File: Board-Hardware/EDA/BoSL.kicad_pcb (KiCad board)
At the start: 2 copper layers, 88 x 69.8 mm, 57 parts, among them CON1 Micro_SD_Card, CON2 BARREL_JACK, IC1 ATMEGA328-P, IC2 SIM7000, J1 Screw_Terminal_1x06, J2 Screw_Terminal_1x04, J3 Screw_Terminal_1x02, J4 Screw_Terminal_1x08, J5 Screw_Terminal_1x04, J6 RJ45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

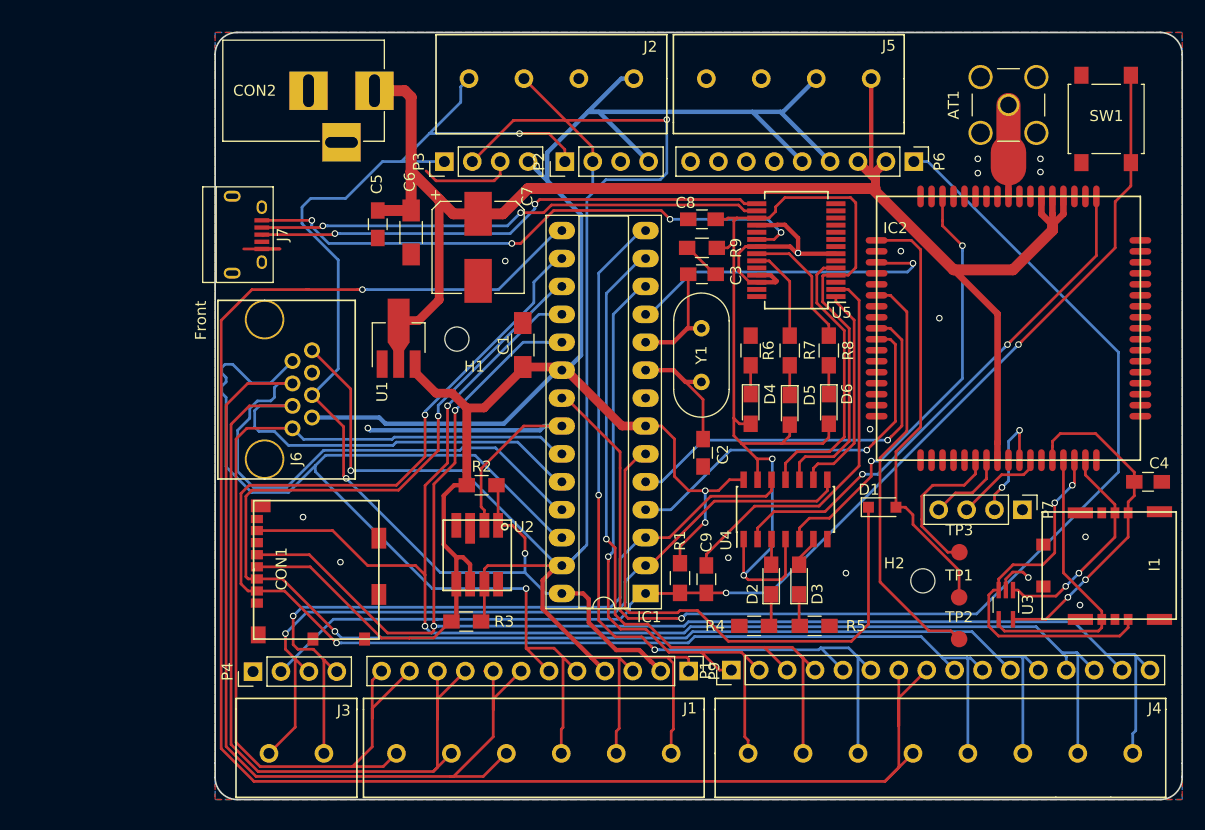
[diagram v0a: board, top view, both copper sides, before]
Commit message: renamed bosl GPS to bosl
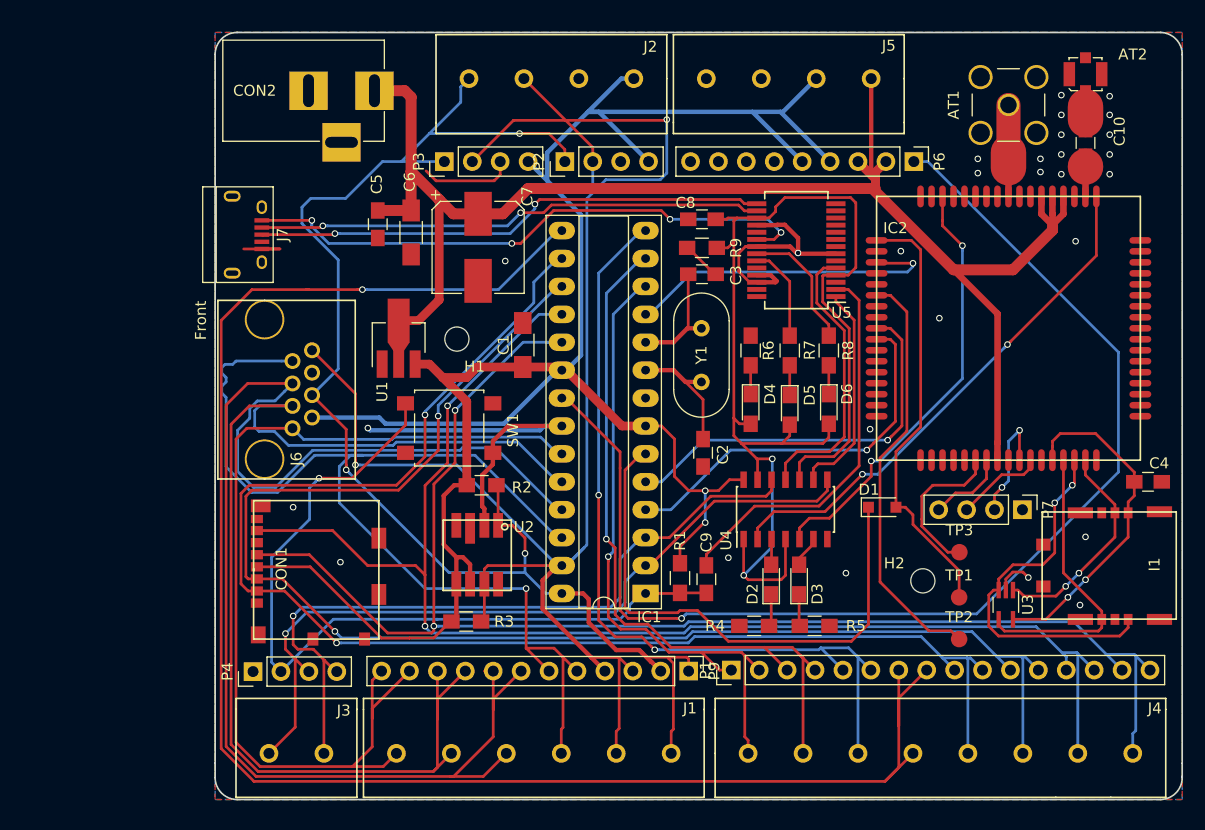
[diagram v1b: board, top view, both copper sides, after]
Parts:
- removed G***: LOGO, SIMFootprints:Logo
- added AT2: AT-GNSS, Connectors_Molex:Molex_Microcoaxial_RF, F.Cu at (183.7, 66.8)
- added C10: 33 pF, Capacitors_SMD:C_0805_HandSoldering, F.Cu at (183.7, 73.0)
- moved SW1 66.1 mm to (125.8, 99.0), turned to 180 degrees
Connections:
- IC2 pad 53: (no net) -> Net-(C10-Pad2)
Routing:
- net TLL_RST: track 108.9 -> 73.9 mm, vias 2 -> 1
- net Net-(C10-Pad2): track 0.00 -> 3.79 mm
- net V_3.3: track 197.0 -> 198.8 mm
- net Net-(AT2-Pad1): track 0.00 -> 1.17 mm
- net GND: track 75.3 -> 76.1 mm, vias 17 -> 28
- net SDA: track 155.6 -> 155.0 mm
- net A3: track 100.9 -> 101.4 mm
- net A2: track 128.5 -> 128.0 mm
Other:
- board text added: "Rev: 0.3 G Monash BoSL GSP Board"
- board text removed: "Rev: 0.3 Monash BoSL Board"

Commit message: begun layout of bosl board rev 0.4
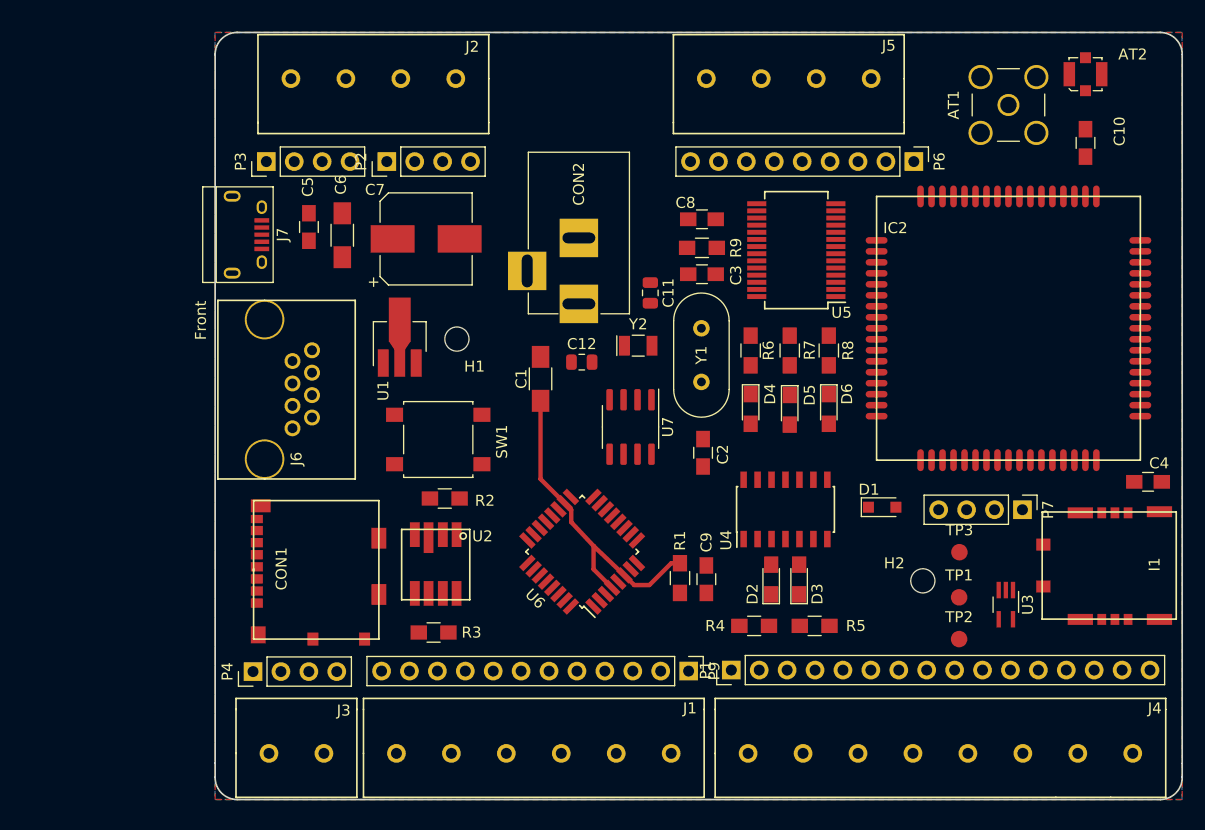
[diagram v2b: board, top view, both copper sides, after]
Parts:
- removed IC1: ATMEGA328-P, Housings_DIP:DIP-28_W7.62mm_Socket_LongPads
- added C11: 12 pF, Capacitor_SMD:C_0805_2012Metric, F.Cu at (144.1, 86.7)
- added C12: 12 pF, Capacitor_SMD:C_0805_2012Metric, F.Cu at (137.9, 93.0)
- added U6: ATmega328P-AU, Package_QFP:TQFP-32_7x7mm_P0.8mm, F.Cu at (137.9, 110.2)
- added U7: MCP7940N-xSN, Package_SO:SOIC-8_3.9x4.9mm_P1.27mm, F.Cu at (142.3, 98.9)
- added Y2: 32.768 kHz, Crystal:Crystal_SMD_EuroQuartz_EQ161-2Pin_3.2x1.5mm, F.Cu at (143.0, 91.5)
- moved CON2 26.9 mm to (137.6, 87.7), turned to 270 degrees
- moved P2 16.2 mm to (120.1, 74.8)
- moved P3 16.2 mm to (109.2, 74.8)
- moved J2 16.2 mm to (126.4, 67.2)
- moved C6 6.27 mm to (116.1, 81.5)
- moved C5 6.27 mm to (113.0, 80.7)
- moved C7 4.79 mm to (123.7, 81.8), turned to 0 degrees
- moved U2 3.87 mm to (124.5, 111.4)
- moved R2 3.57 mm to (125.4, 105.4)
- moved C1 3.48 mm to (134.1, 94.5)
- moved R3 3.13 mm to (124.4, 117.6)
- moved SW1 1.44 mm to (124.8, 100.0)
- moved U1 0.14 mm to (121.3, 91.1)
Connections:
- CON1 pad 1: (no net) -> Net-(CON1-Pad1)
- CON1 pad 8: (no net) -> Net-(CON1-Pad8)
- I1 pad 5: (no net) -> Net-(I1-Pad5)
- IC2 pad 11: (no net) -> Net-(IC2-Pad11)
- IC2 pad 12: (no net) -> Net-(IC2-Pad12)
- IC2 pad 13: (no net) -> Net-(IC2-Pad13)
- IC2 pad 14: (no net) -> Net-(IC2-Pad14)
- IC2 pad 15: (no net) -> Net-(IC2-Pad15)
- IC2 pad 16: (no net) -> Net-(IC2-Pad16)
- IC2 pad 19: (no net) -> Net-(IC2-Pad19)
- IC2 pad 20: (no net) -> Net-(IC2-Pad20)
- IC2 pad 21: (no net) -> Net-(IC2-Pad21)
- IC2 pad 22: (no net) -> Net-(IC2-Pad22)
- IC2 pad 26: (no net) -> Net-(IC2-Pad26)
- IC2 pad 34: (no net) -> Net-(IC2-Pad34)
- IC2 pad 35: (no net) -> Net-(IC2-Pad35)
- IC2 pad 36: (no net) -> Net-(IC2-Pad36)
- IC2 pad 37: (no net) -> Net-(IC2-Pad37)
- IC2 pad 38: (no net) -> Net-(IC2-Pad38)
- IC2 pad 4: (no net) -> Net-(IC2-Pad4)
- IC2 pad 40: (no net) -> Net-(IC2-Pad40)
- IC2 pad 41: (no net) -> Net-(IC2-Pad41)
- IC2 pad 42: (no net) -> Net-(IC2-Pad42)
- IC2 pad 43: (no net) -> Net-(IC2-Pad43)
- IC2 pad 44: (no net) -> Net-(IC2-Pad44)
- IC2 pad 47: (no net) -> Net-(IC2-Pad47)
- IC2 pad 48: (no net) -> Net-(IC2-Pad48)
- IC2 pad 49: (no net) -> Net-(IC2-Pad49)
- IC2 pad 5: (no net) -> Net-(IC2-Pad5)
- IC2 pad 50: (no net) -> Net-(IC2-Pad50)
- IC2 pad 51: (no net) -> Net-(IC2-Pad51)
- IC2 pad 67: (no net) -> Net-(IC2-Pad67)
- IC2 pad 68: (no net) -> Net-(IC2-Pad68)
- IC2 pad 7: (no net) -> Net-(IC2-Pad7)
- IC2 pad 8: (no net) -> Net-(IC2-Pad8)
- J4 pad 1: D6 -> D2
- J4 pad 2: D7 -> D3
- J4 pad 3: D8 -> D6
- J4 pad 4: D9 -> D7
- J7 pad 4: (no net) -> Net-(J7-Pad4)
- J7 pad 6: (no net) -> Net-(J7-Pad6)
- P1 pad 1: D6 -> D2
- P1 pad 2: D6 -> D2
- P1 pad 3: D7 -> D3
- P1 pad 4: D7 -> D3
- P1 pad 5: D8 -> D6
- P1 pad 6: D8 -> D6
- P1 pad 7: D9 -> D7
- P1 pad 8: D9 -> D7
- U2 pad 4: (no net) -> Net-(U2-Pad4)
- U2 pad 8: (no net) -> Net-(U2-Pad8)
- U5 pad 10: (no net) -> Net-(U5-Pad10)
- U5 pad 11: (no net) -> Net-(U5-Pad11)
- U5 pad 12: (no net) -> Net-(U5-Pad12)
- U5 pad 13: (no net) -> Net-(U5-Pad13)
- U5 pad 14: (no net) -> Net-(U5-Pad14)
- U5 pad 19: (no net) -> Net-(U5-Pad19)
- U5 pad 24: (no net) -> Net-(U5-Pad24)
- U5 pad 27: (no net) -> Net-(U5-Pad27)
- U5 pad 28: (no net) -> Net-(U5-Pad28)
- U5 pad 3: (no net) -> Net-(U5-Pad3)
- U5 pad 6: (no net) -> Net-(U5-Pad6)
- U5 pad 8: (no net) -> Net-(U5-Pad8)
- U5 pad 9: (no net) -> Net-(U5-Pad9)
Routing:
- net V_3.3: track 198.8 -> 29.8 mm, vias 2 -> 0
- net D9: track 155.6 -> 0.00 mm, vias 1 -> 0
- net SDA: track 155.0 -> 0.00 mm, vias 2 -> 0
- net VPP: track 147.4 -> 0.00 mm
- net SD_MOSI: track 133.1 -> 0.00 mm, vias 2 -> 0
- net SD_SCLK: track 131.9 -> 0.00 mm, vias 2 -> 0
- net SD_CS: track 131.3 -> 0.00 mm, vias 2 -> 0
- net SCL: track 128.2 -> 0.00 mm, vias 3 -> 0
- net A2: track 128.0 -> 0.00 mm
- net SD_MISO: track 125.7 -> 0.00 mm, vias 2 -> 0
- net TTL_3.3V: track 110.1 -> 0.00 mm, vias 2 -> 0
- net AREF: track 109.6 -> 0.00 mm, vias 1 -> 0
- net A1: track 107.7 -> 0.00 mm
- net A3: track 101.4 -> 0.00 mm, vias 1 -> 0
- net A0: track 90.3 -> 0.00 mm
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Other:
- board text added: "Rev: 0.4 Monash BoSL Board"
- board text removed: "Rev: 0.3 G Monash BoSL GSP Board"

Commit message: finished bosl board rev0.4 layout
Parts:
- C1, C6: footprint Capacitors_SMD:C_1206_HandSoldering -> Capacitor_SMD:C_1206_3216Metric
- C10, C2, C3, C4, C5, C8, C9: footprint Capacitors_SMD:C_0805_HandSoldering -> Capacitor_SMD:C_0805_2012Metric
- D2, D3, D4, D5, D6: footprint LEDs:LED_0805_HandSoldering -> LED_SMD:LED_0805_2012Metric
- R1, R2, R3, R4, R5, R6, R7, R8, R9: footprint Resistors_SMD:R_0805_HandSoldering -> Resistor_SMD:R_0805_2012Metric
- moved C9 19.2 mm to (132.8, 102.8), turned to 0 degrees
- moved R1 18.7 mm to (132.8, 100.2), turned to 180 degrees
- moved R3 12.2 mm to (124.8, 105.4)
- moved R2 12.0 mm to (123.0, 117.2)
- moved C11 3.17 mm to (144.3, 89.9)
- moved Y2 1.80 mm to (143.0, 93.3), turned to 180 degrees
- moved U2 1.46 mm to (126.0, 111.4), turned to 90 degrees
- moved R4 1.45 mm to (154.2, 115.7)
- moved R5 1.40 mm to (158.5, 115.7)
- moved C12 1.24 mm to (139.1, 93.3)
- moved C6 0.31 mm to (116.1, 81.2)
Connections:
- J7 pad 6: Net-(J7-Pad6) -> (no net)
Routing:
- net V_3.3: track 29.8 -> 232.0 mm, vias 0 -> 4
- net SCL: track 0.00 -> 181.5 mm, vias 0 -> 2
- net SD_MISO: track 0.00 -> 155.2 mm, vias 0 -> 2
- net SD_MOSI: track 0.00 -> 141.9 mm, vias 0 -> 2
- net VPP: track 0.00 -> 138.2 mm, vias 0 -> 1
- net SD_CS: track 0.00 -> 131.3 mm, vias 0 -> 2
- net SDA: track 0.00 -> 123.6 mm, vias 0 -> 4
- net SD_SCLK: track 0.00 -> 103.3 mm, vias 0 -> 3
- net A2: track 0.00 -> 89.0 mm, vias 0 -> 1
- net A1: track 0.00 -> 82.4 mm, vias 0 -> 1
- net TLL_RX: track 0.00 -> 82.4 mm, vias 0 -> 2
- net A3: track 0.00 -> 82.2 mm, vias 0 -> 3
- net A0: track 0.00 -> 80.3 mm, vias 0 -> 1
- net TTL_3.3V: track 0.00 -> 78.3 mm, vias 0 -> 2
- net GND: track 0.00 -> 77.2 mm, vias 0 -> 19
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
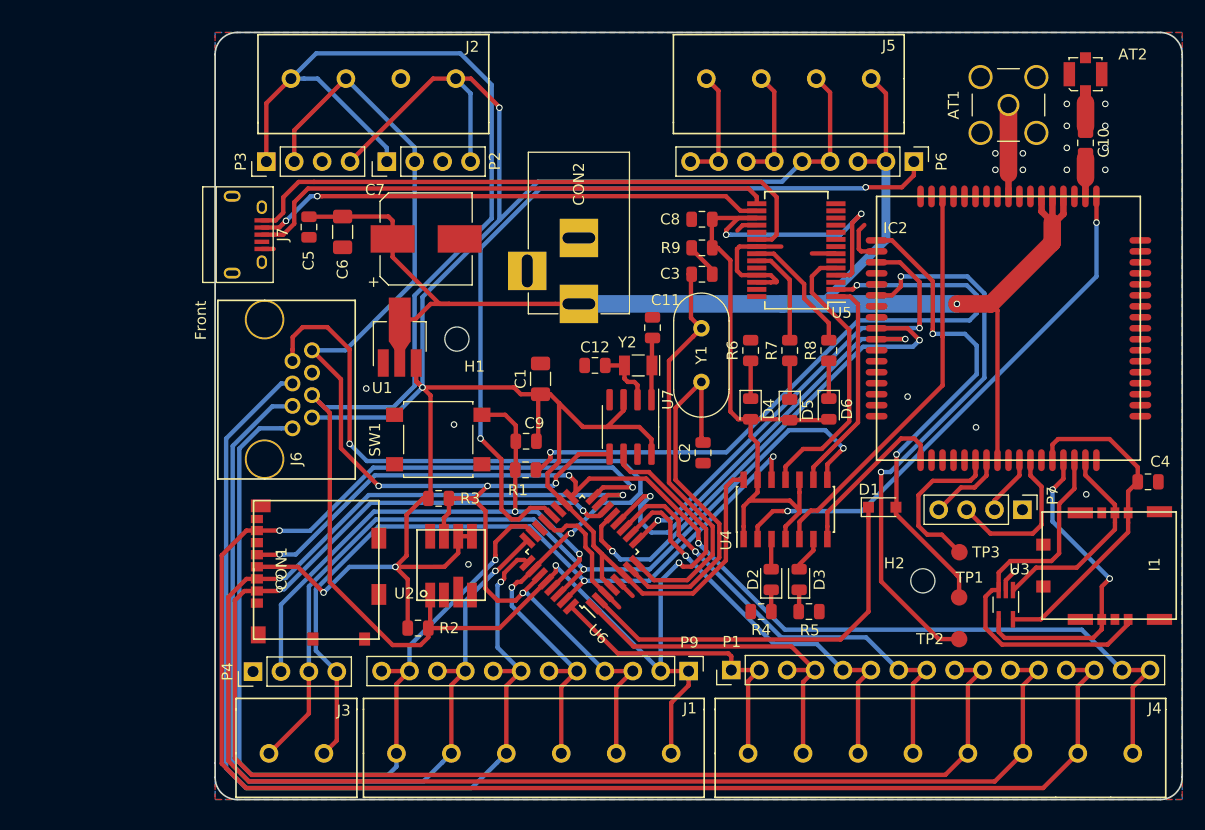
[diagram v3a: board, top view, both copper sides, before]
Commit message: added  update layout for bosl v4
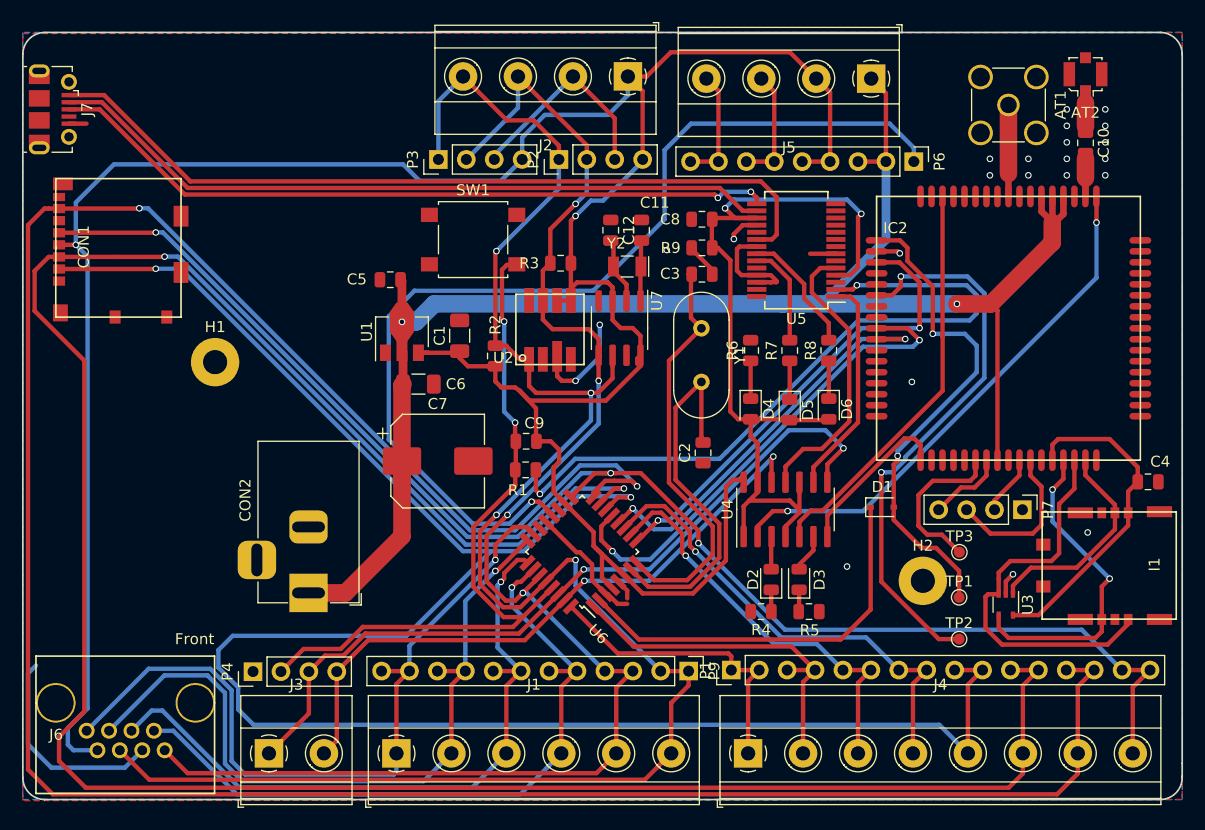
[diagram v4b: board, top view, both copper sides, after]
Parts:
- AT1: footprint Connectors:SMA_THT_Jack_Straight -> Connector_Coaxial:SMA_Amphenol_901-144_Vertical
- AT2: footprint Connectors_Molex:Molex_Microcoaxial_RF -> Connector_Coaxial:U.FL_Molex_MCRF_73412-0110_Vertical
- C7: footprint Capacitors_SMD:CP_Elec_8x10 -> Capacitor_SMD:CP_Elec_8x10
- CON2: footprint Connectors:BARREL_JACK -> Connector_BarrelJack:BarrelJack_Horizontal
- D1: footprint Diodes_SMD:D_SOD-323_HandSoldering -> Diode_SMD:D_SOD-323
- H1, H2: footprint Mounting_Holes:MountingHole_2.2mm_M2 -> MountingHole:MountingHole_2.2mm_M2_Pad
- J1: footprint SIMFootprints:Screw_Terminals_1x6 -> TerminalBlock_Phoenix:TerminalBlock_Phoenix_MKDS-1,5-6_1x06_P5.00mm_Horizontal
- J2, J5: footprint SIMFootprints:Screw_Terminals_1x4 -> TerminalBlock_Phoenix:TerminalBlock_Phoenix_MKDS-1,5-4_1x04_P5.00mm_Horizontal
- J3: footprint SIMFootprints:Screw_Terminals_1x2 -> TerminalBlock_Phoenix:TerminalBlock_Phoenix_MKDS-1,5-2_1x02_P5.00mm_Horizontal
- J4: footprint SIMFootprints:Screw_Terminals_1x8 -> TerminalBlock_Phoenix:TerminalBlock_Phoenix_MKDS-1,5-8_1x08_P5.00mm_Horizontal
- J7: footprint Connectors:USB_Micro-B -> Connector_USB:USB_Micro-B_Molex-105017-0001
- P1: footprint Pin_Headers:Pin_Header_Straight_1x16_Pitch2.54mm -> Connector_PinHeader_2.54mm:PinHeader_1x16_P2.54mm_Vertical
- P2, P3, P4, P7: footprint Pin_Headers:Pin_Header_Straight_1x04_Pitch2.54mm -> Connector_PinHeader_2.54mm:PinHeader_1x04_P2.54mm_Vertical
- P6: footprint Pin_Headers:Pin_Header_Straight_1x09_Pitch2.54mm -> Connector_PinHeader_2.54mm:PinHeader_1x09_P2.54mm_Vertical
- P9: footprint Pin_Headers:Pin_Header_Straight_1x12_Pitch2.54mm -> Connector_PinHeader_2.54mm:PinHeader_1x12_P2.54mm_Vertical
- SW1: footprint Buttons_Switches_SMD:SW_SPST_B3S-1000 -> Button_Switch_SMD:SW_SPST_B3S-1000
- TP1, TP2, TP3: footprint Measurement_Points:Measurement_Point_Round-SMD-Pad_Small -> TestPoint:TestPoint_Pad_D1.0mm
- U1: footprint TO_SOT_Packages_SMD:SOT-89-3_Handsoldering -> Package_TO_SOT_SMD:SOT-89-3
- U3: footprint TO_SOT_Packages_SMD:SOT-353_SC-70-5_Handsoldering -> Package_TO_SOT_SMD:SOT-353_SC-70-5
- U4: footprint Housings_SOIC:SOIC-14_3.9x8.7mm_Pitch1.27mm -> Package_SO:SOIC-14_3.9x8.7mm_P1.27mm
- U5: footprint Housings_SSOP:SSOP-28_5.3x10.2mm_Pitch0.65mm -> Package_SO:SSOP-28_5.3x10.2mm_P0.65mm
- Y1: footprint Crystals:Crystal_HC49-U_Vertical -> Crystal:Crystal_HC49-4H_Vertical
- moved CON2 36.0 mm to (113.0, 114.0)
- moved J6 35.4 mm to (102.7, 124.0), turned to 180 degrees
- moved CON1 34.4 mm to (90.0, 82.5)
- moved R2 25.7 mm to (130.0, 92.4), turned to 90 degrees
- moved R3 24.1 mm to (135.9, 84.0), turned to 180 degrees
- moved U2 23.3 mm to (135.0, 90.0)
- moved H1 22.1 mm to (104.5, 93.0)
- moved J7 21.0 mm to (89.7, 70.0)
- moved C7 20.2 mm to (124.8, 102.0)
- moved SW1 18.5 mm to (128.0, 81.8), turned to 0 degrees
- moved P2 15.7 mm to (135.8, 74.6)
- moved J2 15.7 mm to (142.1, 67.0)
- moved P3 15.7 mm to (124.8, 74.6)
- moved C6 15.5 mm to (123.0, 95.0), turned to 0 degrees
- moved C12 12.4 mm to (140.5, 81.0), turned to 270 degrees
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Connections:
- J7 pad 6: (no net) -> Net-(J7-Pad6)
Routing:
- net SD_MISO: track 155.2 -> 235.8 mm
- net SD_MOSI: track 141.9 -> 219.1 mm
- net SD_CS: track 131.3 -> 181.0 mm
- net GND: track 77.2 -> 122.4 mm, vias 19 -> 23
- net SD_SCLK: track 103.3 -> 134.6 mm
- net A2: track 89.0 -> 63.6 mm
- net V_3.3: track 232.0 -> 255.9 mm, vias 4 -> 2
- net USB_DM: track 46.8 -> 66.7 mm, vias 2 -> 0
- net USB_V: track 55.1 -> 73.7 mm
- net USB_DP: track 48.9 -> 66.9 mm, vias 0 -> 2
- net AREF: track 73.7 -> 91.6 mm, vias 2 -> 1
- net A3: track 82.2 -> 64.4 mm, vias 3 -> 1
- net SDA: track 123.6 -> 138.3 mm
- net A1: track 82.4 -> 68.1 mm
- net SCL: track 181.5 -> 167.3 mm, vias 2 -> 4
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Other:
- board size 88 x 69.8 mm -> 105.5 x 69.8 mm

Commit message: added revision of bosl board
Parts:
- added BT1: Battery_Cell, SIMFootprints:2996TR, B.Cu at (181.3, 92.6)
- AT1, CON2, J6: moved to B.Cu
- moved H1 38.5 mm to (142.6, 98.6)
- moved J7 29.7 mm to (119.1, 65.7), turned to 180 degrees
- moved CON2 24.7 mm to (110.3, 89.4), turned to 180 degrees
- moved J6 24.3 mm to (113.7, 102.3), turned to 270 degrees
- moved CON1 17.2 mm to (105.7, 75.4)
- turned AT1 to 90 degrees
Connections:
- J7 pad 6: Net-(J7-Pad6) -> (no net)
- U7 pad 3: V_3.3 -> Net-(BT1-Pad1)
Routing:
- net Net-(BT1-Pad1): track 0.00 -> 73.3 mm, vias 0 -> 1
- net SD_MISO: track 235.8 -> 203.7 mm
- net SD_MOSI: track 219.1 -> 187.9 mm
- net V_3.3: track 255.9 -> 226.7 mm, vias 2 -> 3
- net AREF: track 91.6 -> 117.6 mm
- net USB_V: track 73.7 -> 48.8 mm
- net USB_DM: track 66.7 -> 42.8 mm
- net A1: track 68.1 -> 44.7 mm, vias 1 -> 2
- net A0: track 71.0 -> 47.7 mm, vias 1 -> 2
- net USB_DP: track 66.9 -> 44.1 mm
- net A2: track 63.6 -> 45.3 mm, vias 1 -> 2
- net A3: track 64.4 -> 48.0 mm, vias 1 -> 2
- net GND: track 122.4 -> 106.0 mm, vias 23 -> 26
- net SDA: track 138.3 -> 154.5 mm
- net SCL: track 167.3 -> 173.7 mm
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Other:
- board size 105.5 x 69.8 mm -> 88 x 69.8 mm
